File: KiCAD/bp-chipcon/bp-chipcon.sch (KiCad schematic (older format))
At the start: 21 parts

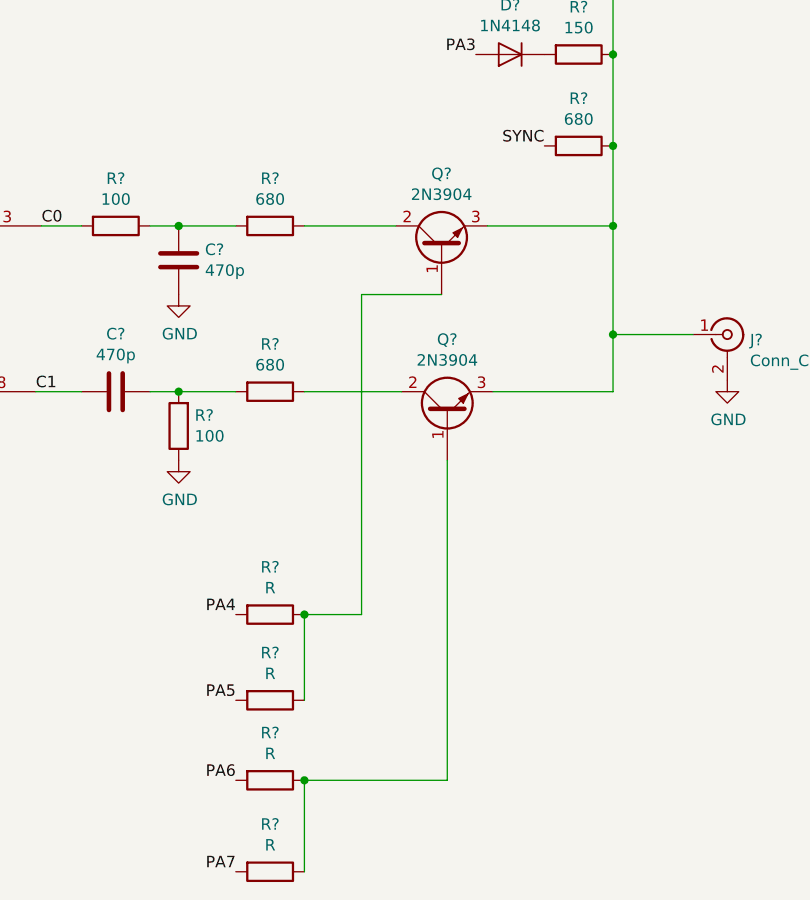
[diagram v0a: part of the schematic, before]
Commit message: working on schematic and color scheme
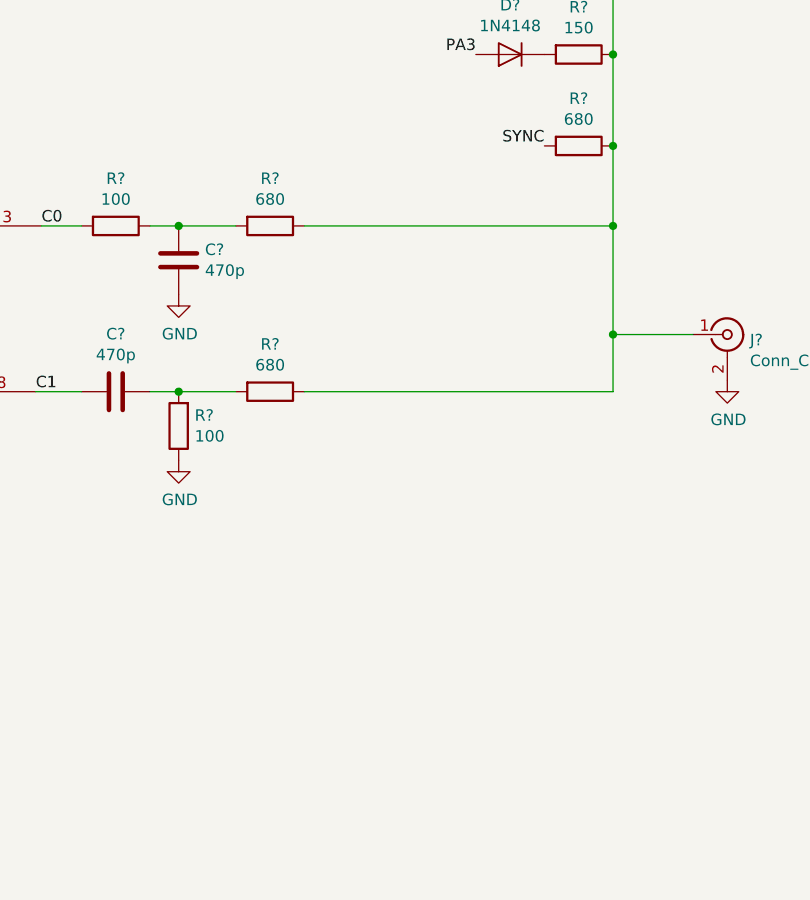
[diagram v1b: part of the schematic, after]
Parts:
- removed Q? (x2): 2N3904, symbol device:Q_NPN_BCE
- removed R? (x4): R, symbol device:R
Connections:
- net at J?.1 (In), R?.1, R?.1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: now also R?.1, R?.1
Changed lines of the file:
@@
 EESchema Schematic File Version 4
+LIBS:bp-chipcon-cache
 EELAYER 26 0
 EELAYER END
@@
 	-1   0    0    1
 $EndComp
-$Comp
-L device:Q_NPN_BCE Q?
-U 1 1 5CD39D35
-P 8375 2500
-F 0 "Q?" V 8703 2500 50  0000 C CNN
-F 1 "2N3904" V 8612 2500 50  0000 C CNN
-F 2 "" H 8575 2600 50  0001 C CNN
-F 3 "" H 8375 2500 50  0001 C CNN
-	1    8375 2500
-	0    -1   -1   0
-$EndComp
-$Comp
-L device:Q_NPN_BCE Q?
-U 1 1 5CD3A00A
-P 8400 3225
-F 0 "Q?" V 8728 3225 50  0000 C CNN
-F 1 "2N3904" V 8637 3225 50  0000 C CNN
-F 2 "" H 8600 3325 50  0001 C CNN
-F 3 "" H 8400 3225 50  0001 C CNN
-	1    8400 3225
-	0    -1   -1   0
-$EndComp
-Wire Wire Line
-	7775 3125 8200 3125
 Wire Wire Line
 	9125 2050 9125 2400
 Wire Wire Line
-	8600 3125 9125 3125
-Wire Wire Line
 	9125 2875 9125 3125
-Wire Wire Line
-	7775 2400 8175 2400
-Wire Wire Line
-	8575 2400 9125 2400
 Connection ~ 9125 2400
 Wire Wire Line
 	9125 2400 9125 2875
-$Comp
-L device:R R?
-U 1 1 5CD3A3F1
-P 7625 4100
-F 0 "R?" V 7418 4100 50  0000 C CNN
-F 1 "R" V 7509 4100 50  0000 C CNN
-F 2 "" V 7555 4100 50  0001 C CNN
-F 3 "" H 7625 4100 50  0001 C CNN
-	1    7625 4100
-	0    1    1    0
-$EndComp
-$Comp
-L device:R R?
-U 1 1 5CD3A66A
-P 7625 4475
-F 0 "R?" V 7418 4475 50  0000 C CNN
-F 1 "R" V 7509 4475 50  0000 C CNN
-F 2 "" V 7555 4475 50  0001 C CNN
-F 3 "" H 7625 4475 50  0001 C CNN
-	1    7625 4475
-	0    1    1    0
-$EndComp
-$Comp
-L device:R R?
-U 1 1 5CD3A6C6
-P 7625 4825
-F 0 "R?" V 7418 4825 50  0000 C CNN
-F 1 "R" V 7509 4825 50  0000 C CNN
-F 2 "" V 7555 4825 50  0001 C CNN
-F 3 "" H 7625 4825 50  0001 C CNN
-	1    7625 4825
-	0    1    1    0
-$EndComp
-$Comp
-L device:R R?
-U 1 1 5CD3A750
-P 7625 5225
-F 0 "R?" V 7418 5225 50  0000 C CNN
-F 1 "R" V 7509 5225 50  0000 C CNN
-F 2 "" V 7555 5225 50  0001 C CNN
-F 3 "" H 7625 5225 50  0001 C CNN
-	1    7625 5225
-	0    1    1    0
-$EndComp
-Wire Wire Line
-	7775 4100 7775 4475
-Wire Wire Line
-	7775 4825 7775 5225
-Wire Wire Line
-	7775 4825 8400 4825
-Wire Wire Line
-	8400 4825 8400 3425
-Connection ~ 7775 4825
-Wire Wire Line
-	7775 4100 8025 4100
-Wire Wire Line
-	8025 4100 8025 2700
-Wire Wire Line
-	8025 2700 8375 2700
-Connection ~ 7775 4100
-Text Label 7475 4100 2    50   ~ 0
-PA4
-Text Label 7475 4475 2    50   ~ 0
-PA5
-Text Label 7475 5225 2    50   ~ 0
-PA7
-Text Label 7475 4825 2    50   ~ 0
-PA6
 Text Label 3825 3300 2    50   ~ 0
 PA3
@@
 Text Label 3825 3700 2    50   ~ 0
 PA7
+Wire Wire Line
+	7775 2400 9125 2400
+Wire Wire Line
+	7775 3125 9125 3125
 $EndSCHEMATC

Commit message: work on tvout
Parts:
- added C1: 100n, symbol device:C
- gave numbers to parts that had none: 14
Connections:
- net C1: now also U1.6 (OUT); no longer U1.8 (OUT)
- net GND: now also C1.2
- net PA1: now also U1.4 (IN1); no longer U1.9 (IN1)
- net PB1: now also U1.5 (IN2); no longer U1.10 (IN2)
- new net U1-pin14: C1.1
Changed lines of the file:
@@
 $EndDescr
 $Comp
-L Personal_KiCAD:BLUE_PILL M?
+L Personal_KiCAD:BLUE_PILL M1
 U 1 1 5CD2DE62
 P 4325 3550
-F 0 "M?" H 4325 5278 50  0000 C CNN
+F 0 "M1" H 4325 5278 50  0000 C CNN
 F 1 "BLUE_PILL" H 4325 5187 50  0000 C CNN
 F 2 "" H 4325 3550 50  0001 C CNN
@@
 $EndComp
 $Comp
-L 74xx:74HC86 U?
+L 74xx:74HC86 U1
 U 1 1 5CD37862
 P 6025 2400
-F 0 "U?" H 6025 2806 50  0000 C CNN
+F 0 "U1" H 6025 2806 50  0000 C CNN
 F 1 "74HC86" H 6025 2715 50  0000 C CNN
 F 2 "" H 6025 2400 50  0001 C CNN
@@
 $EndComp
 $Comp
-L 74xx:74HC86 U?
-U 3 1 5CD37A4A
+L 74xx:74HC86 U1
+U 2 1 5CD37A4A
 P 6000 3125
-F 0 "U?" H 6000 3531 50  0000 C CNN
+F 0 "U1" H 6000 3531 50  0000 C CNN
 F 1 "74HC86" H 6000 3440 50  0000 C CNN
 F 2 "" H 6000 3125 50  0001 C CNN
 F 3 "" H 6000 3125 50  0001 C CNN
-	3    6000 3125
+	2    6000 3125
 	1    0    0    -1
 $EndComp
@@
 C1
 $Comp
-L device:R R?
+L device:R R4
 U 1 1 5CD37BF4
 P 6950 2400
-F 0 "R?" V 6743 2400 50  0000 C CNN
+F 0 "R4" V 6743 2400 50  0000 C CNN
 F 1 "100" V 6834 2400 50  0000 C CNN
 F 2 "" V 6880 2400 50  0001 C CNN
@@
 $EndComp
 $Comp
-L device:R R?
+L device:R R7
 U 1 1 5CD37C69
 P 7225 3275
-F 0 "R?" H 7155 3229 50  0000 R CNN
+F 0 "R7" H 7155 3229 50  0000 R CNN
 F 1 "100" H 7155 3320 50  0000 R CNN
 F 2 "" V 7155 3275 50  0001 C CNN
@@
 $EndComp
 $Comp
-L device:C C?
+L device:C C2
 U 1 1 5CD37CF7
 P 7225 2550
-F 0 "C?" H 7340 2596 50  0000 L CNN
+F 0 "C2" H 7340 2596 50  0000 L CNN
 F 1 "470p" H 7340 2505 50  0000 L CNN
 F 2 "" H 7263 2400 50  0001 C CNN
@@
 $EndComp
 $Comp
-L power:GND #PWR?
+L power:GND #PWR02
 U 1 1 5CD37E21
 P 7225 2700
-F 0 "#PWR?" H 7225 2450 50  0001 C CNN
+F 0 "#PWR02" H 7225 2450 50  0001 C CNN
 F 1 "GND" H 7230 2527 50  0000 C CNN
 F 2 "" H 7225 2700 50  0001 C CNN
@@
 $EndComp
 $Comp
-L device:C C?
+L device:C C3
 U 1 1 5CD37F5C
 P 6950 3125
-F 0 "C?" V 6698 3125 50  0000 C CNN
+F 0 "C3" V 6698 3125 50  0000 C CNN
 F 1 "470p" V 6789 3125 50  0000 C CNN
 F 2 "" H 6988 2975 50  0001 C CNN
@@
 $EndComp
 $Comp
-L power:GND #PWR?
+L power:GND #PWR04
 U 1 1 5CD3805D
 P 7225 3425
-F 0 "#PWR?" H 7225 3175 50  0001 C CNN
+F 0 "#PWR04" H 7225 3175 50  0001 C CNN
 F 1 "GND" H 7230 3252 50  0000 C CNN
 F 2 "" H 7225 3425 50  0001 C CNN
@@
 	7100 2400 7225 2400
 $Comp
-L conn:Conn_Coaxial J?
+L conn:Conn_Coaxial J1
 U 1 1 5CD3812E
 P 9625 2875
-F 0 "J?" H 9724 2851 50  0000 L CNN
+F 0 "J1" H 9724 2851 50  0000 L CNN
 F 1 "Conn_Coaxial" H 9724 2760 50  0000 L CNN
 F 2 "" H 9625 2875 50  0001 C CNN
@@
 $EndComp
 $Comp
-L power:GND #PWR?
+L power:GND #PWR03
 U 1 1 5CD38290
 P 9625 3075
-F 0 "#PWR?" H 9625 2825 50  0001 C CNN
+F 0 "#PWR03" H 9625 2825 50  0001 C CNN
 F 1 "GND" H 9630 2902 50  0000 C CNN
 F 2 "" H 9625 3075 50  0001 C CNN
@@
 $EndComp
 $Comp
-L device:R R?
+L device:R R5
 U 1 1 5CD382D8
 P 7625 2400
-F 0 "R?" V 7418 2400 50  0000 C CNN
+F 0 "R5" V 7418 2400 50  0000 C CNN
 F 1 "680" V 7509 2400 50  0000 C CNN
 F 2 "" V 7555 2400 50  0001 C CNN
@@
 $EndComp
 $Comp
-L device:R R?
+L device:R R6
 U 1 1 5CD38346
 P 7625 3125
-F 0 "R?" V 7418 3125 50  0000 C CNN
+F 0 "R6" V 7418 3125 50  0000 C CNN
 F 1 "680" V 7509 3125 50  0000 C CNN
 F 2 "" V 7555 3125 50  0001 C CNN
@@
 Connection ~ 9125 2875
 $Comp
-L device:R R?
+L device:R R3
 U 1 1 5CD384CE
 P 8975 2050
-F 0 "R?" V 8768 2050 50  0000 C CNN
+F 0 "R3" V 8768 2050 50  0000 C CNN
 F 1 "680" V 8859 2050 50  0000 C CNN
 F 2 "" V 8905 2050 50  0001 C CNN
@@
 SYNC
 $Comp
-L device:R R?
+L device:R R2
 U 1 1 5CD3871B
 P 8975 1650
-F 0 "R?" V 8768 1650 50  0000 C CNN
+F 0 "R2" V 8768 1650 50  0000 C CNN
 F 1 "150" V 8859 1650 50  0000 C CNN
 F 2 "" V 8905 1650 50  0001 C CNN
@@
 PA2
 $Comp
-L device:D D?
+L device:D D2
 U 1 1 5CD389F6
 P 8675 1650
-F 0 "D?" H 8675 1434 50  0000 C CNN
+F 0 "D2" H 8675 1434 50  0000 C CNN
 F 1 "1N4148" H 8675 1525 50  0000 C CNN
 F 2 "" H 8675 1650 50  0001 C CNN
@@
 PA2
 $Comp
-L device:R R?
+L device:R R1
 U 1 1 5CD38F49
 P 8975 1300
-F 0 "R?" V 8768 1300 50  0000 C CNN
+F 0 "R1" V 8768 1300 50  0000 C CNN
 F 1 "300" V 8859 1300 50  0000 C CNN
 F 2 "" V 8905 1300 50  0001 C CNN
@@
 	9125 1650 9125 2050
 $Comp
-L device:D D?
+L device:D D1
 U 1 1 5CD39683
 P 8675 1300
-F 0 "D?" H 8675 1084 50  0000 C CNN
+F 0 "D1" H 8675 1084 50  0000 C CNN
 F 1 "1N4148" H 8675 1175 50  0000 C CNN
 F 2 "" H 8675 1300 50  0001 C CNN
@@
 Wire Wire Line
 	7775 3125 9125 3125
+$Comp
+L device:C C1
+U 1 1 5CD58135
+P 5800 1475
+F 0 "C1" H 5915 1521 50  0000 L CNN
+F 1 "100n" H 5915 1430 50  0000 L CNN
+F 2 "" H 5838 1325 50  0001 C CNN
+F 3 "" H 5800 1475 50  0001 C CNN
+	1    5800 1475
+	1    0    0    -1
+$EndComp
+$Comp
+L power:GND #PWR01
+U 1 1 5CD5834F
+P 5800 1625
+F 0 "#PWR01" H 5800 1375 50  0001 C CNN
+F 1 "GND" H 5805 1452 50  0000 C CNN
+F 2 "" H 5800 1625 50  0001 C CNN
+F 3 "" H 5800 1625 50  0001 C CNN
+	1    5800 1625
+	1    0    0    -1
+$EndComp
+Text Label 5800 1325 0    50   ~ 0
+U1-pin14
 $EndSCHEMATC

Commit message: modification to schematic
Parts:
- removed U1: 74HC86, symbol 74xx:74HC86
- added BT?: Battery, symbol device:Battery
- added C2: 100n, symbol device:C
- added C?: 10µF/16v, symbol device:CP
- added D?: 1N4148, symbol device:D
- added Q1, Q2: 2N7000, TO_SOT_Packages_THT:TO-92_Molded_Narrow, symbol transistors:2N7000
- added R8: 75, symbol device:R
- added SW?: power, symbol switches:SW_DPST_x2
- added SW?: LEFT, symbol switches:SW_Push
- added SW?: RIGHT, symbol switches:SW_Push
- added SW?: UP, symbol switches:SW_Push
- added SW?: DOWN, symbol switches:SW_Push
- added SW?: A, symbol switches:SW_Push
- added SW?: B, symbol switches:SW_Push
- added U1: 74HC86N, symbol Personal_KiCAD:74HC86N
- added U2: CD74HC4002, symbol Personal_KiCAD:CD74HC4002
- renumbered C2 to C3, C3 to C4
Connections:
- net C0: now also U1.3
- net C1: now also U1.6
- net GND: now also BT?.2 (-), C2.2, C?.2, Q1.1 (S), Q2.1 (S), R8.2, SW?.1, SW?.1, SW?.1, SW?.1, SW?.1, SW?.2, U1.10, U1.12, U1.13, U1.9, U2.10, U2.11, U2.12, U2.9
- net PA0: now also U1.2, U2.2
- net PA1: now also U1.4, U2.3
- net PA2: now also U2.4
- net PA3: now also U2.5
- net PA4: now also SW?.2
- net PA5: now also SW?.2
- net PA6: now also SW?.2
- net PA7: now also SW?.1
- net PB0: now also U1.1
- net PB1: now also U1.5
- net PA14: now reaches M1.23 (PB_14)
- net PA14: now also SW?.2
- net PA15: now reaches M1.30 (PA_15)
- net PA15: now also SW?.2
- net at C3.1, R4.1, R5.2: now also Q1.3 (D)
- net at C4.1, R6.2, R7.2: now also Q2.3 (D)
- net at J1.1 (In), R1.1, R2.1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: now also R8.1
- new net: Q1.2 (G), Q2.2 (G), U2.1
- new net: BT?.1 (+), SW?.1 (A)
- new net: D?.2 (A), SW?.2 (B)
- new net 3.3V: C?.1, D?.1 (K)
- new net U2-pin14: C2.1
- no-connect marks 0 -> 3
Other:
- note added: "3xAAA\nNiMh"
- note added: "Vbat\n4volt\n"
- note added: "block chroma\nwhen all output\nare zero"
- moved on the sheet: R5, R6

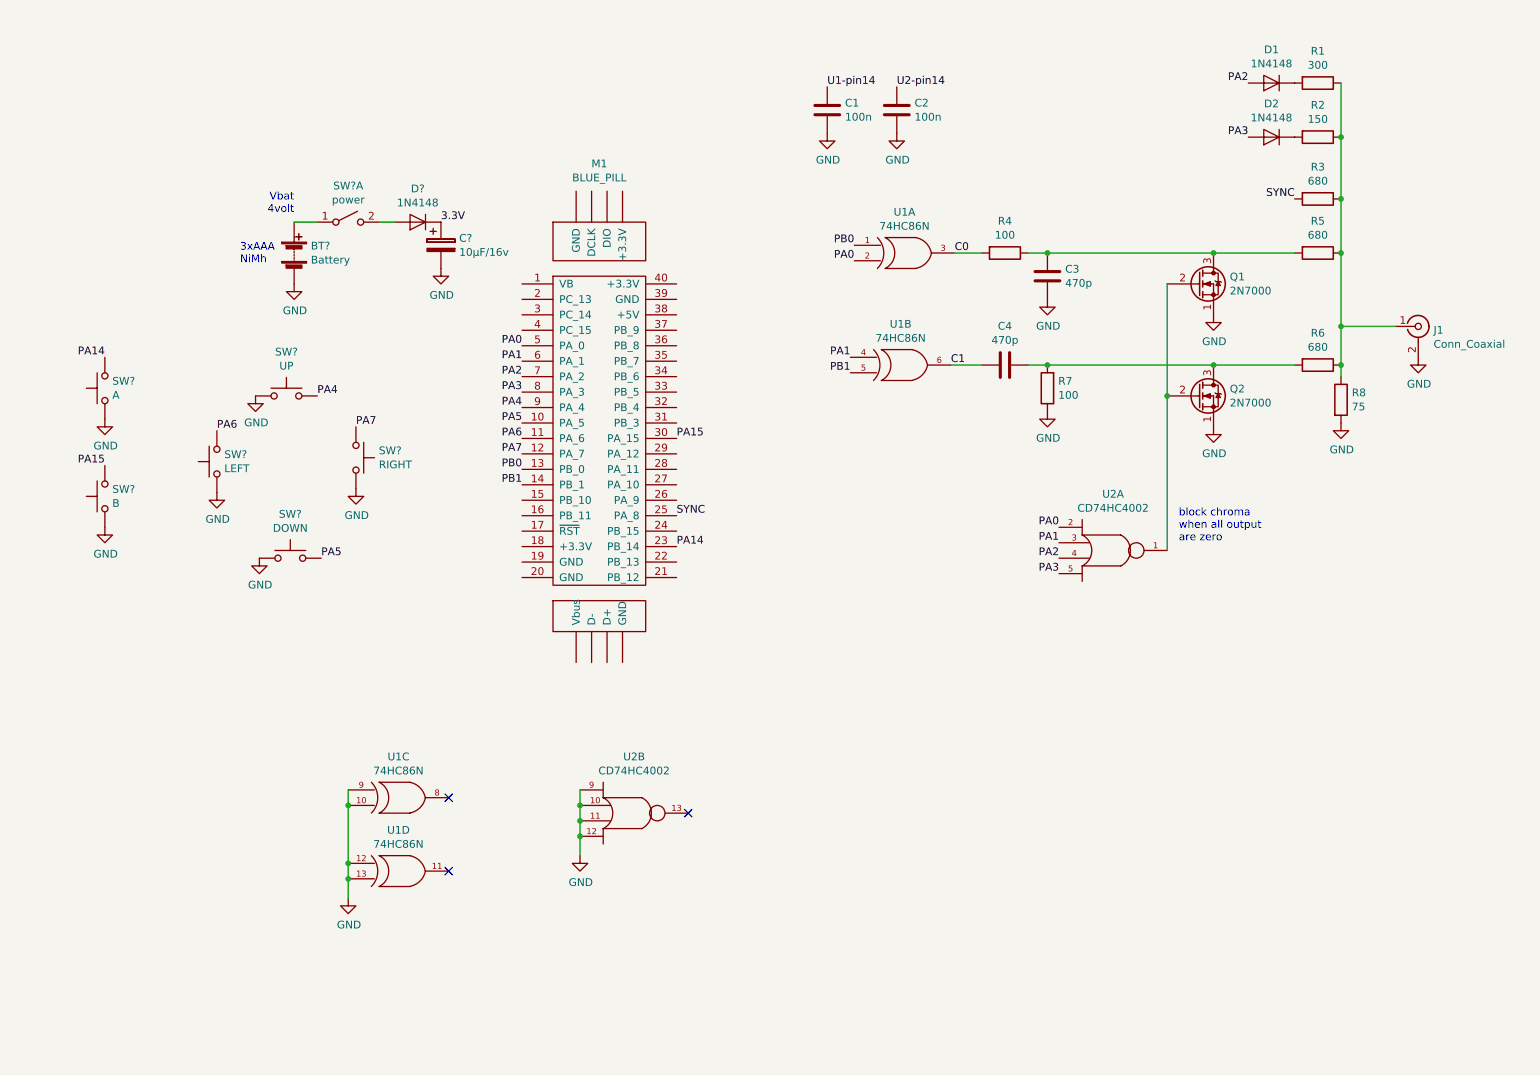
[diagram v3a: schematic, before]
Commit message: Added video modes CHIP8, SCHIP, XOCHIP
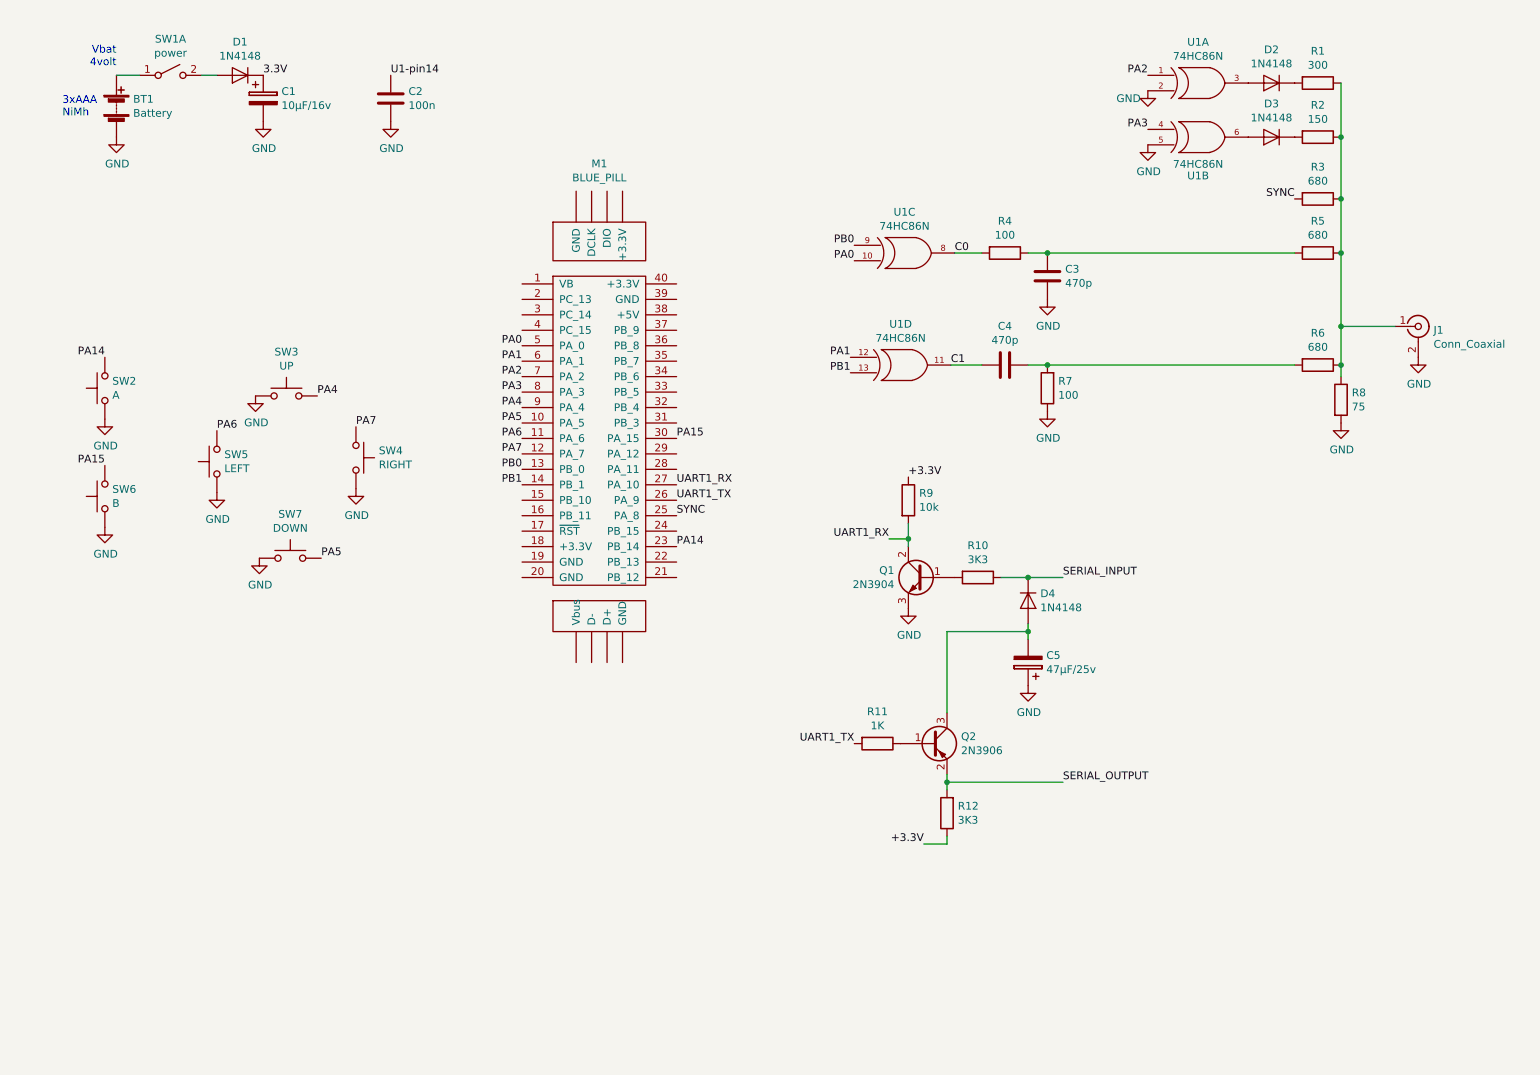
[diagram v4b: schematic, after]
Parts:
- removed C2: 100n, symbol device:C
- removed Q1, Q2: 2N7000, TO_SOT_Packages_THT:TO-92_Molded_Narrow, symbol transistors:2N7000
- removed U2: CD74HC4002, symbol Personal_KiCAD:CD74HC4002
- added C5: 47µF/25v, symbol device:CP
- added D4: 1N4148, symbol device:D
- added Q1: 2N3904, symbol device:Q_NPN_BCE
- added Q2: 2N3906, symbol device:Q_PNP_BEC
- added R10, R12: 3K3, symbol device:R
- added R11: 1K, symbol device:R
- added R9: 10k, symbol device:R
- gave numbers to parts that had none: 10
- renumbered C1 to C2, D1 to D2, D2 to D3
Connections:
- net C0: now also U1.8; no longer U1.3
- net C1: now also U1.11; no longer U1.6
- net GND: now also U1.2, U1.5, C5.1, Q1.3 (E); no longer U1.10, U1.12, U1.13, U1.9
- net PA0: now also U1.10; no longer U1.2
- net PA1: now also U1.12; no longer U1.4
- net PA2: now also U1.1; no longer D2.2 (A)
- net PA3: now also U1.4; no longer D3.2 (A)
- net PB0: now also U1.9; no longer U1.1
- net PB1: now also U1.13; no longer U1.5
- net UART1_TX: now reaches M1.26 (PA_9)
- net UART1_TX: now also R11.2
- net UART1_RX: now reaches M1.27 (PA_10)
- net UART1_RX: now also Q1.2 (C), R9.2
- new net: D3.2 (A), U1.6
- new net: D2.2 (A), U1.3
- new net: Q1.1 (B), R10.2
- new net: C5.2, D4.2 (A), Q2.3 (C)
- new net: Q2.1 (B), R11.1
- new net +3.3V: R12.1, R9.1
- new net SERIAL_INPUT: D4.1 (K), R10.1
- new net SERIAL_OUTPUT: Q2.2 (E), R12.2
- no-connect marks 3 -> 0
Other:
- note removed: "block chroma\nwhen all output\nare zero"
- moved on the sheet: BT1, C1, C2, D1, SW1A
